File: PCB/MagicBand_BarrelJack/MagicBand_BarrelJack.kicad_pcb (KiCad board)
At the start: 2 copper layers, 40 x 40 mm, 22 parts, among them J2 PinSocket_1x08_P2.54mm_Vertic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, J3 PinHeader_1x03_P2.54mm_Vertic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, J6 JST_PH_B3B-PH-K_1x03_P2.00mm_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, J8 PinHeader_1x02_P2.54mm_Vertic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, J9 IDC-Header_2x03_P2.54mm_Verti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, Q1 SOT-23, U1 DIP-28_W7.62mm, U2 SOT-23, Y1 Crystal_HC49-4H_Vertical

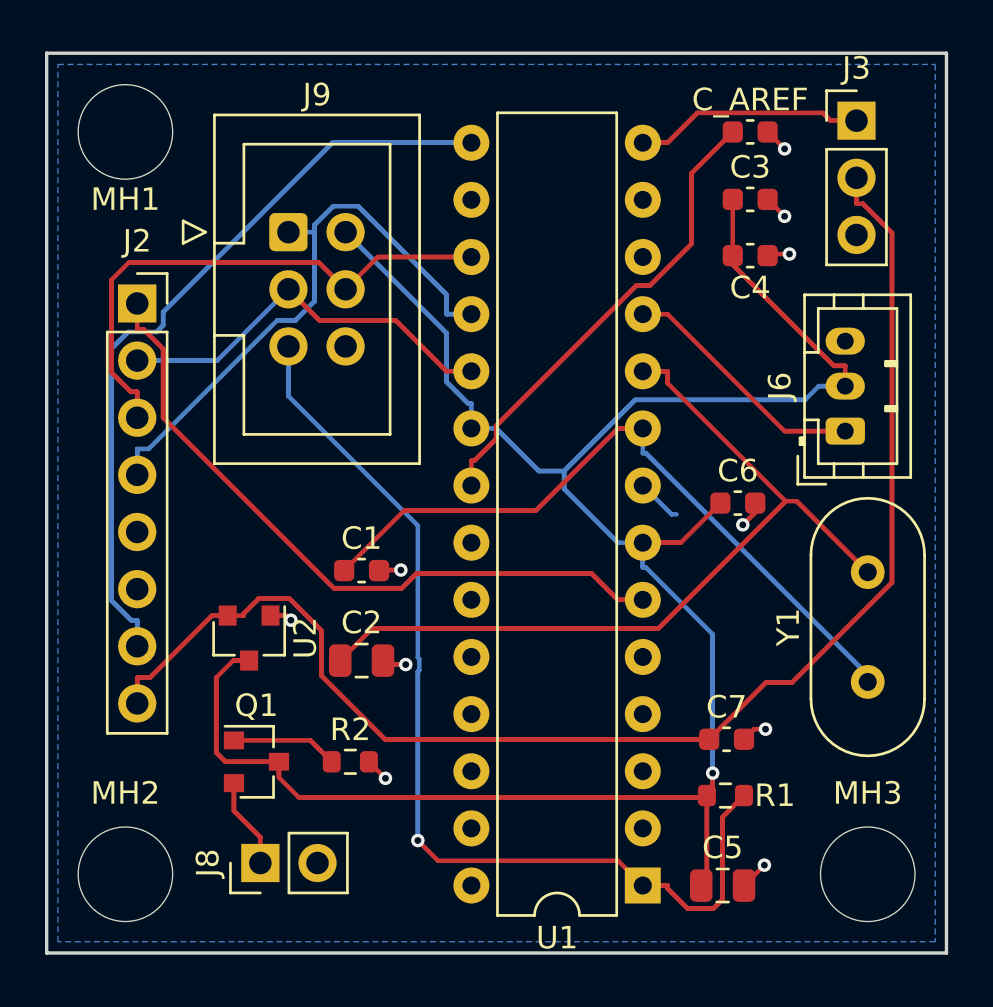
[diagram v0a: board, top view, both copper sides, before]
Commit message: Center U1, fix orientation-label text height, widen mounting-hole margin
Applied PDR should-fix items: bumped "Right"/"Top" silkscreen labels
to 1mm height (was 0.75mm, under the min-text-height rule and typical
fab legibility floor -- stroke width left at 0.1mm, not bumped to the
recommended 0.15mm, worth revisiting); re-centered U1 for max edge
clearance both directions (front/back placement constraint deemed not
load-bearing here, per user); moved MH1-3 for ~2.4mm min edge margin
(up from ~1.4mm).

Cleared all tracks/vias for the U1 move, re-ran FreeRouting (42 -> 0
unrouted, ~2.3s), imported, refilled.

DRC: U1 pad 8 (starved-thermal/isolated island) and U1 pad 22
(unconnected) recurred -- same category of issue as previous passes,
now at U1's new position. New: a silk_overlap between the "Right"
label and U1's own silkscreen outline, introduced by the move. 3
pre-existing footprint-library warnings unchanged.

RF antenna proximity issue from the PDR (GND pour/vias too close to
J3) explicitly deferred per user decision -- noted, not fixed, revisit
if real-world range issues arise.
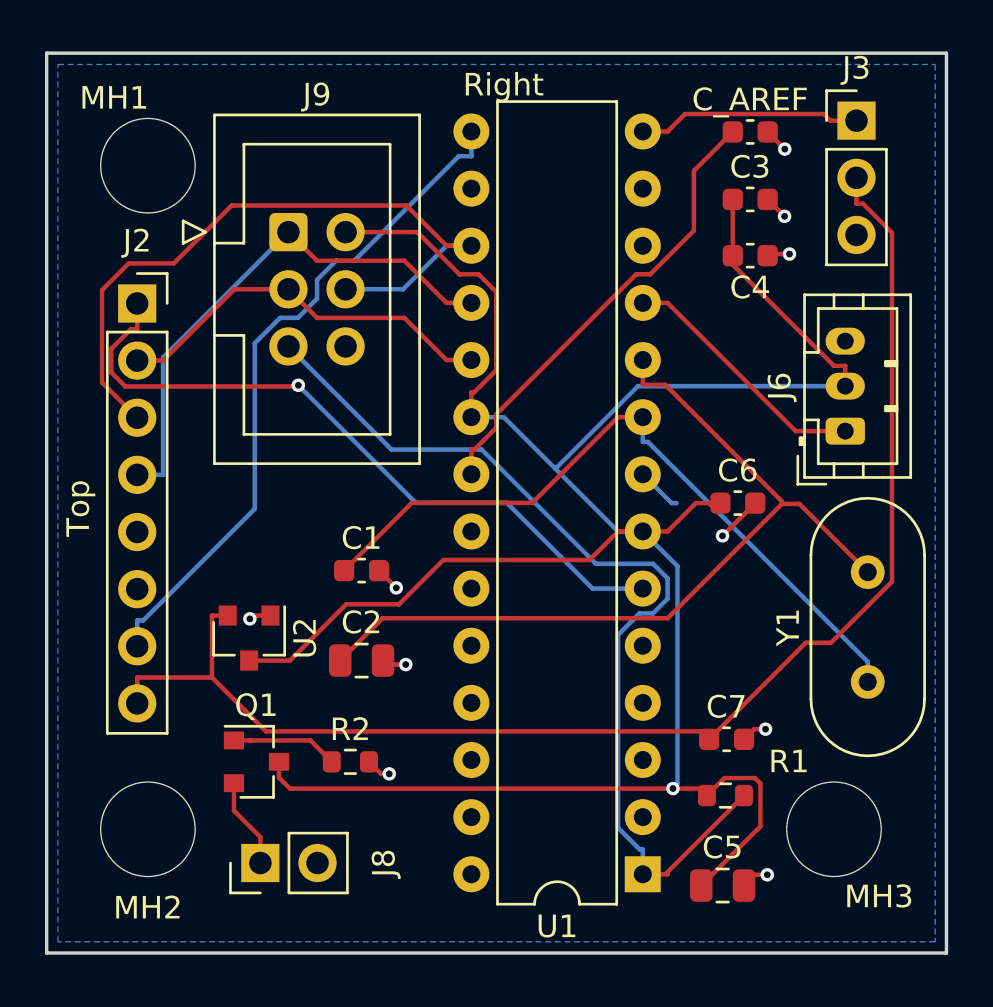
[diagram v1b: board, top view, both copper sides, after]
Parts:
- moved MH3 2.50 mm to (35.0, 34.5)
- moved MH2 2.24 mm to (4.50, 34.5)
- moved MH1 1.80 mm to (4.50, 5.00)
- moved U1 0.50 mm to (26.5, 36.5)
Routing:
- net +3V3: track 122.0 -> 61.0 mm
- net +5V: track 173.1 -> 113.2 mm
- net D9: track 66.7 -> 30.5 mm
- net D4: track 60.7 -> 31.4 mm, vias 0 -> 1
- net Net-(U1-XTAL2/PB7): track 63.5 -> 37.1 mm
- net Net-(U1-XTAL1/PB6): track 57.8 -> 32.1 mm
- net MCU_RESET: track 63.4 -> 42.1 mm, vias 1 -> 0
- net Net-(U1-AREF): track 40.8 -> 20.5 mm
- net D12: track 41.4 -> 23.7 mm
- net D11: track 45.2 -> 31.4 mm
- net D13: track 29.8 -> 17.5 mm
- net D8: track 14.8 -> 9.95 mm
- net GND: track 16.9 -> 13.9 mm
- net Net-(J8-Pin_1): track 6.92 -> 4.04 mm
- net D5: track 13.9 -> 11.4 mm
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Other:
- board text added: "Right"
- board text added: "Top"

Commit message: U1 pad 8 and pad 22 bridged again, board DRC-clean except cosmetics
Manual GND bridge tracks at U1's new (centered) position, same fix
as before. DRC: 5 -> 3 violations, 1 -> 0 unconnected. Only the 3
pre-existing footprint-library path warnings remain (MH1-3, cosmetic,
not fixable from the GUI). The silk_overlap between the "Right" label
and U1's outline from the recenter is also gone.
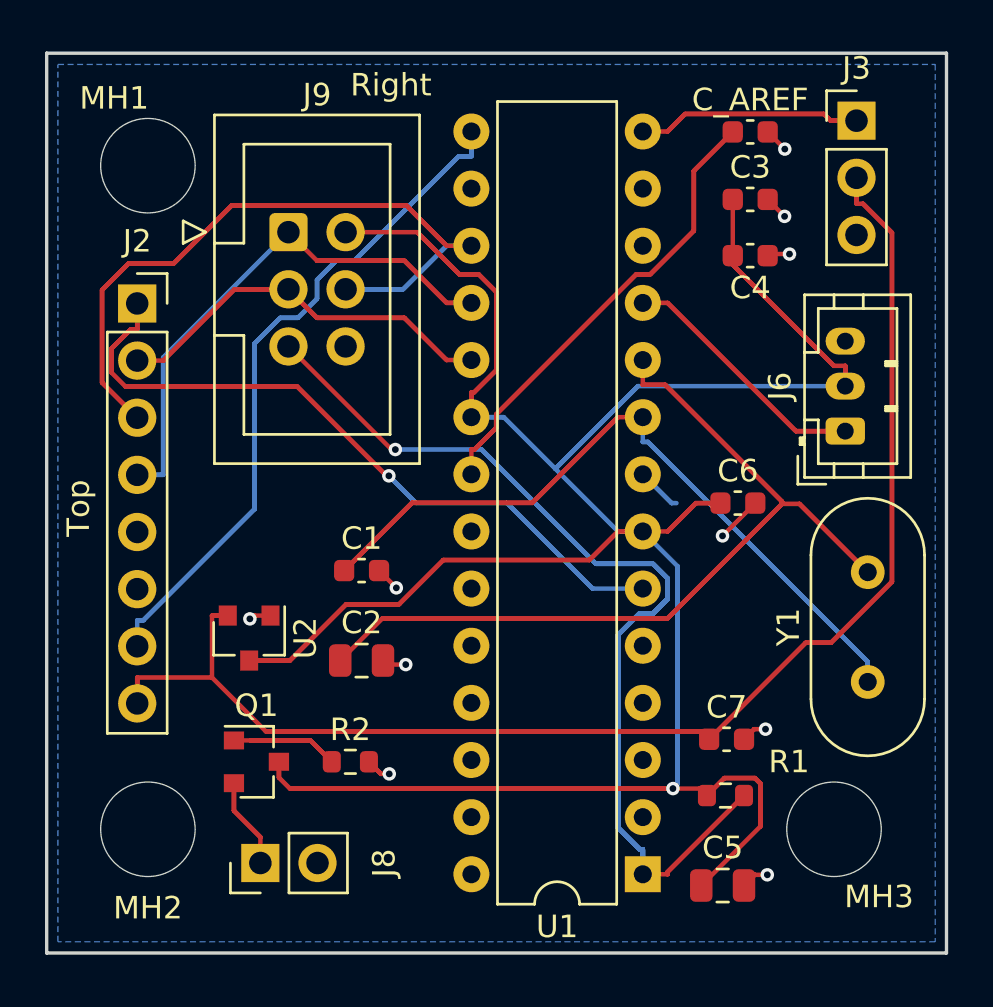
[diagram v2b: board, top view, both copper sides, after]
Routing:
- net MCU_RESET: track 42.1 -> 177.7 mm, vias 0 -> 1
- net +5V: track 113.2 -> 193.8 mm
- net +3V3: track 61.0 -> 112.2 mm
- net Net-(U1-XTAL2/PB7): track 37.1 -> 69.7 mm
- net Net-(U1-XTAL1/PB6): track 32.1 -> 62.1 mm
- net D9: track 30.5 -> 59.8 mm
- net D11: track 31.4 -> 60.7 mm
- net D4: track 31.4 -> 59.5 mm
- net Net-(U1-AREF): track 20.5 -> 39.9 mm
- net D13: track 17.5 -> 32.7 mm
- net D12: track 23.7 -> 37.7 mm
- net D5: track 11.4 -> 21.6 mm
- net D8: track 9.95 -> 18.8 mm
- net GND: track 13.9 -> 18.4 mm
- net Net-(Q1-Pin_1): track 4.74 -> 8.74 mm
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
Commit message: Y1 relocated for edge clearance, manual track cleanup, board reconnected
User moved Y1 (crystal) off the right edge (was ~0.70mm margin, flagged
by PDR #3) and manually cleaned up duplicate tracks + finished routing
by hand -- no FreeRouting import used this round, all done directly in
the GUI.

DRC: 0 unconnected pads. 4 violations remain: 3 pre-existing cosmetic
footprint-library warnings, 1 residual starved-thermal flag on U1 pad
8 (same cosmetic-only situation confirmed previously -- net is
electrically complete).
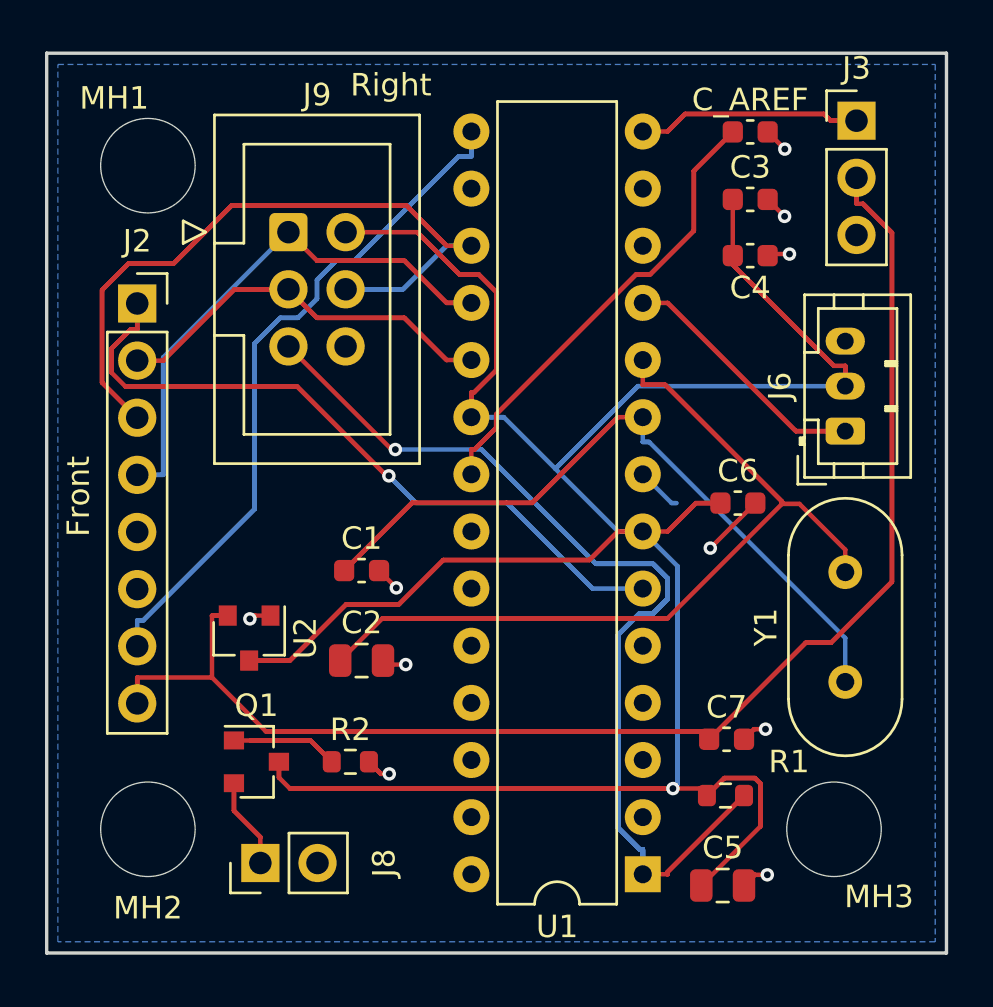
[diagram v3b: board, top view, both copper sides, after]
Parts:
- moved Y1 1.00 mm to (35.5, 27.9)
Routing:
- net Net-(U1-XTAL1/PB6): track 62.1 -> 47.0 mm
- net Net-(U1-XTAL2/PB7): track 69.7 -> 57.8 mm
- net GND: track 18.4 -> 17.4 mm
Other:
- board text added: "Front"
- board text removed: "Top"
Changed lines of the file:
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@@
 	(footprint "Crystal_HC49-4H_Vertical"
 		(layer "F.Cu")
-		(at 36.5 27.95 90)
+		(at 35.5 27.95 90)
 		(descr "Crystal THT HC-49-4H http://5hertz.com/pdfs/04404_D.pdf")
 		(tags "THT crystalHC-49-4H")
@@
 			(remove_unused_layers no)
 			(net "unconnected-(U1-PD0-Pad2)")
-			(zone_connect 2)
 		)
 		(pad "3" thru_hole oval
@@
 		)
 	)
-	(gr_text "Top"
+	(gr_text "Front"
 		(at 2 21.5 90)
 		(layer "F.SilkS")
@@
 	)
 	(segment
-		(start 30.0434 21.4566)
-		(end 31.5 20)
-		(width 0.2)
-		(layer "F.Cu")
-		(net "GND")
-	)
-	(segment
 		(start 32.0344 36.523)
 		(end 31.477 36.523)
@@
 	)
 	(segment
+		(start 29.5 22)
+		(end 31.5 20)
+		(width 0.2)
+		(layer "F.Cu")
+		(net "GND")
+	)
+	(segment
 		(start 14.775 23)
 		(end 15.5426 23.7676)
@@
 	)
 	(via
-		(at 30.0434 21.4566)
+		(at 29.5 22)
 		(size 0.6)
 		(drill 0.3)
@@
 	)
 	(segment
-		(start 26.5 18.72)
-		(end 27.78 20)
-		(width 0.2)
-		(layer "B.Cu")
-		(net "GND")
-	)
-	(segment
 		(start 27.78 20)
 		(end 26.5 18.72)
@@
 	)
 	(segment
-		(start 33.4641 20.0341)
-		(end 36.5 23.07)
+		(start 35.5 22.07)
+		(end 33.4641 20.0341)
+		(width 0.2)
+		(layer "F.Cu")
+		(net "Net-(U1-XTAL2{slash}PB7)")
+	)
+	(segment
+		(start 35.5 23.07)
+		(end 35.5 22.07)
 		(width 0.2)
 		(layer "F.Cu")
@@
 	)
 	(segment
-		(start 27.6048 25.1187)
-		(end 32.6894 20.0341)
-		(width 0.2)
-		(layer "F.Cu")
-		(net "Net-(U1-XTAL2{slash}PB7)")
-	)
-	(segment
 		(start 14.9313 25.1187)
 		(end 27.6048 25.1187)
@@
 	)
 	(segment
-		(start 33.4641 20.0341)
-		(end 36.5 23.07)
-		(width 0.2)
-		(layer "F.Cu")
-		(net "Net-(U1-XTAL2{slash}PB7)")
-	)
-	(segment
 		(start 13.05 27)
 		(end 14.9313 25.1187)
@@
 	)
 	(segment
-		(start 36.5 27.0534)
-		(end 36.5 27.95)
+		(start 35.5 26)
+		(end 35.5 27.95)
 		(width 0.2)
 		(layer "B.Cu")
@@
 	)
 	(segment
-		(start 26.7283 17.2817)
-		(end 36.5 27.0534)
+		(start 26.7817 17.2817)
+		(end 35.5 26)
 		(width 0.2)
 		(layer "B.Cu")
@@
 	)
 	(segment
-		(start 26.5 16.18)
-		(end 26.5 17.2817)
+		(start 26.7283 17.2817)
+		(end 26.7817 17.2817)
 		(width 0.2)
 		(layer "B.Cu")
@@
 	)
 	(segment
-		(start 36.5 27.0534)
-		(end 26.7283 17.2817)
+		(start 26.5 16.18)
+		(end 26.5 17.2817)
 		(width 0.2)
 		(layer "B.Cu")
@@
 		(width 0.2)
 		(layer "B.Cu")
-		(net "Net-(U1-XTAL1{slash}PB6)")
-	)
-	(segment
-		(start 36.5 27.95)
-		(end 36.5 27.0534)
-		(width 0.2)
-		(layer "B.Cu")

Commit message: Remove 183 duplicate track segments via Route > Cleanup Tracks and Vias
A programmatic scan (start/end/layer/net comparison) found roughly
half the board's routing existed as exact duplicate overlapping
segments -- 183 of 367 total, far more than the single duplicate at
U1 pad 8 caught by PDR #3. Likely accumulated across several
FreeRouting-import + manual-routing passes where new tracks were
added alongside old ones instead of replacing them.

Cleanup run with "delete redundant tracks" + "merge co-linear
segments" + "delete dangling tracks" enabled. Verified: 367 -> 183
segments, 0 duplicates remaining. DRC unchanged (0 unconnected pads,
4 harmless violations) -- connectivity fully intact.
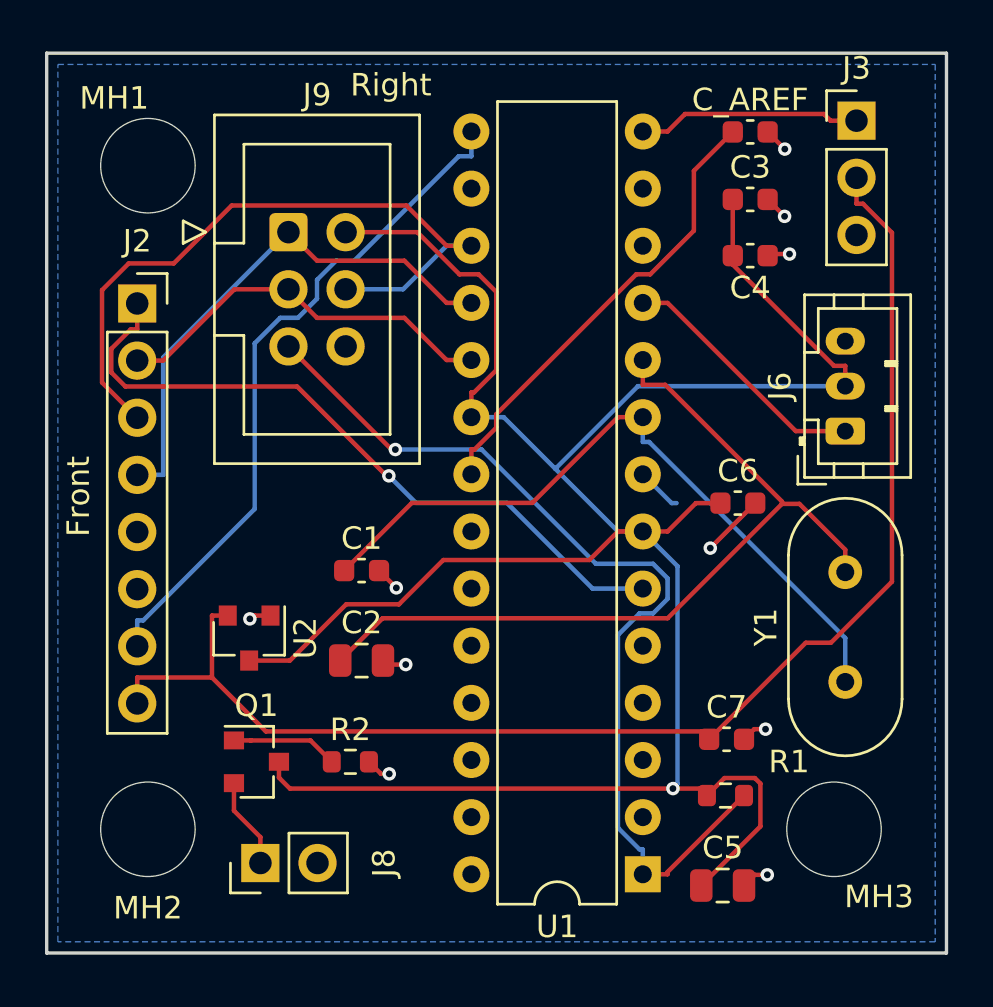
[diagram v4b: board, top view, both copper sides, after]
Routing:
- net MCU_RESET: track 177.7 -> 42.1 mm
- net +5V: track 193.8 -> 113.2 mm
- net +3V3: track 112.2 -> 61.0 mm
- net D9: track 59.8 -> 30.5 mm
- net D11: track 60.7 -> 31.4 mm
- net D4: track 59.5 -> 31.3 mm
- net Net-(U1-XTAL2/PB7): track 57.8 -> 36.7 mm
- net Net-(U1-AREF): track 39.9 -> 20.5 mm
- net Net-(U1-XTAL1/PB6): track 47.0 -> 31.8 mm
- net D13: track 32.7 -> 17.5 mm
- net D12: track 37.7 -> 23.7 mm
- net D5: track 21.6 -> 11.4 mm
- net D8: track 18.8 -> 9.95 mm
- net Net-(Q1-Pin_1): track 8.74 -> 4.74 mm
- net Net-(J8-Pin_1): track 6.92 -> 4.04 mm
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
